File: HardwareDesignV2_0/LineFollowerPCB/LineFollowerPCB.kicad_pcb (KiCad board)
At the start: 2 copper layers, 152 x 100 mm, 11 parts, among them J1 B2B-XH-A, J2 B4B-XH-A, J3 Conn_01x04, M1 Motor_DC, M2 Motor_DC, U1 Black Pill v2, U2 DRV8833, U3 AMS1117-3.3, U4 SX1308

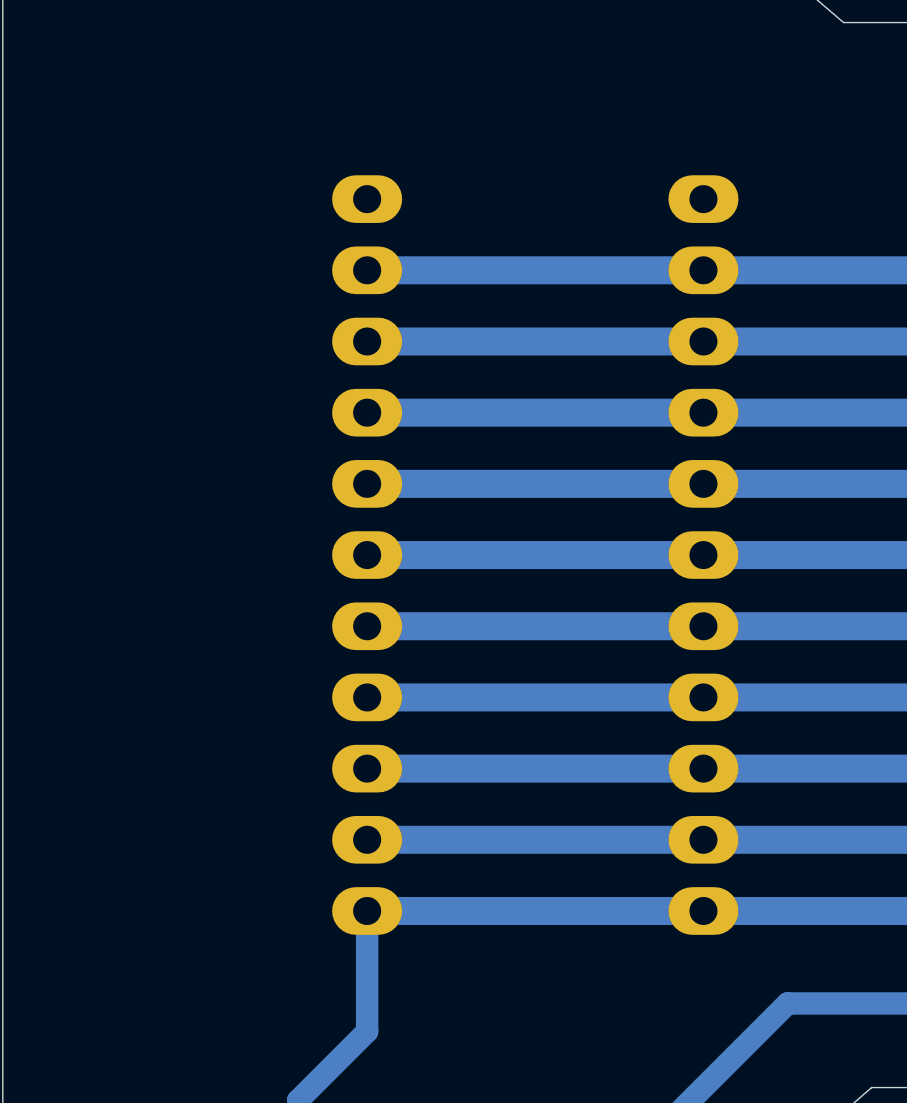
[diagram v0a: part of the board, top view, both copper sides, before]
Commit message: The LineFollower PCB design Version 2.0 with Cytron sensor
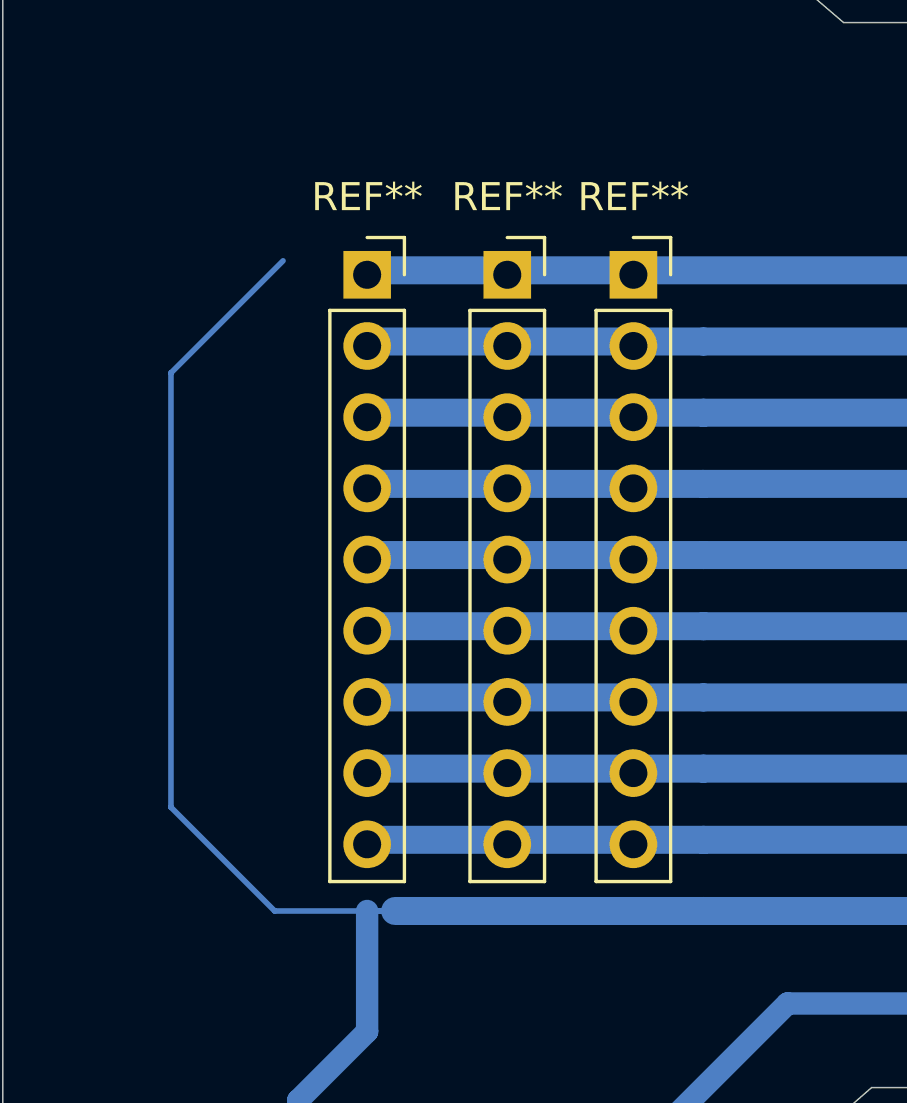
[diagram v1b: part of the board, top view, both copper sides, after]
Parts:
- removed U5, U6: ~, Connector_PinHeader_2.54mm:PinHeader_1x11_P2.54mm_Vertical
- added REF**: PinSocket_1x09_P2.54mm_Vertical, Connector_PinSocket_2.54mm:PinSocket_1x09_P2.54mm_Vertical, F.Cu at (88.0, 79.0)
- added REF**: PinSocket_1x09_P2.54mm_Vertical, Connector_PinSocket_2.54mm:PinSocket_1x09_P2.54mm_Vertical, F.Cu at (92.5, 79.0)
- added REF**: PinSocket_1x09_P2.54mm_Vertical, Connector_PinSocket_2.54mm:PinSocket_1x09_P2.54mm_Vertical, F.Cu at (83.0, 79.0)
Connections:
- U1 pad 26: IR_SG -> VCC
- U1 pad 27: D1 -> GND
- U1 pad 28: D2 -> AN
- U1 pad 29: D3 -> CAL
- U1 pad 30: D4 -> D1
- U1 pad 31: D5 -> D2
- U1 pad 32: D6 -> D3
- U1 pad 33: D7 -> D4
- U1 pad 34: D8 -> D5
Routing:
- net VCC: track 0.00 -> 90.5 mm
- net IR_SG: track 90.5 -> 0.00 mm
- net GND: track 0.00 -> 90.5 mm
- net D8: track 90.5 -> 0.00 mm
- net D7: track 90.5 -> 0.00 mm
- net D6: track 90.5 -> 0.00 mm
- net CAL: track 0.00 -> 90.5 mm
- net AN: track 0.00 -> 90.5 mm
- net IR_3.3V: track 122.3 -> 153.0 mm

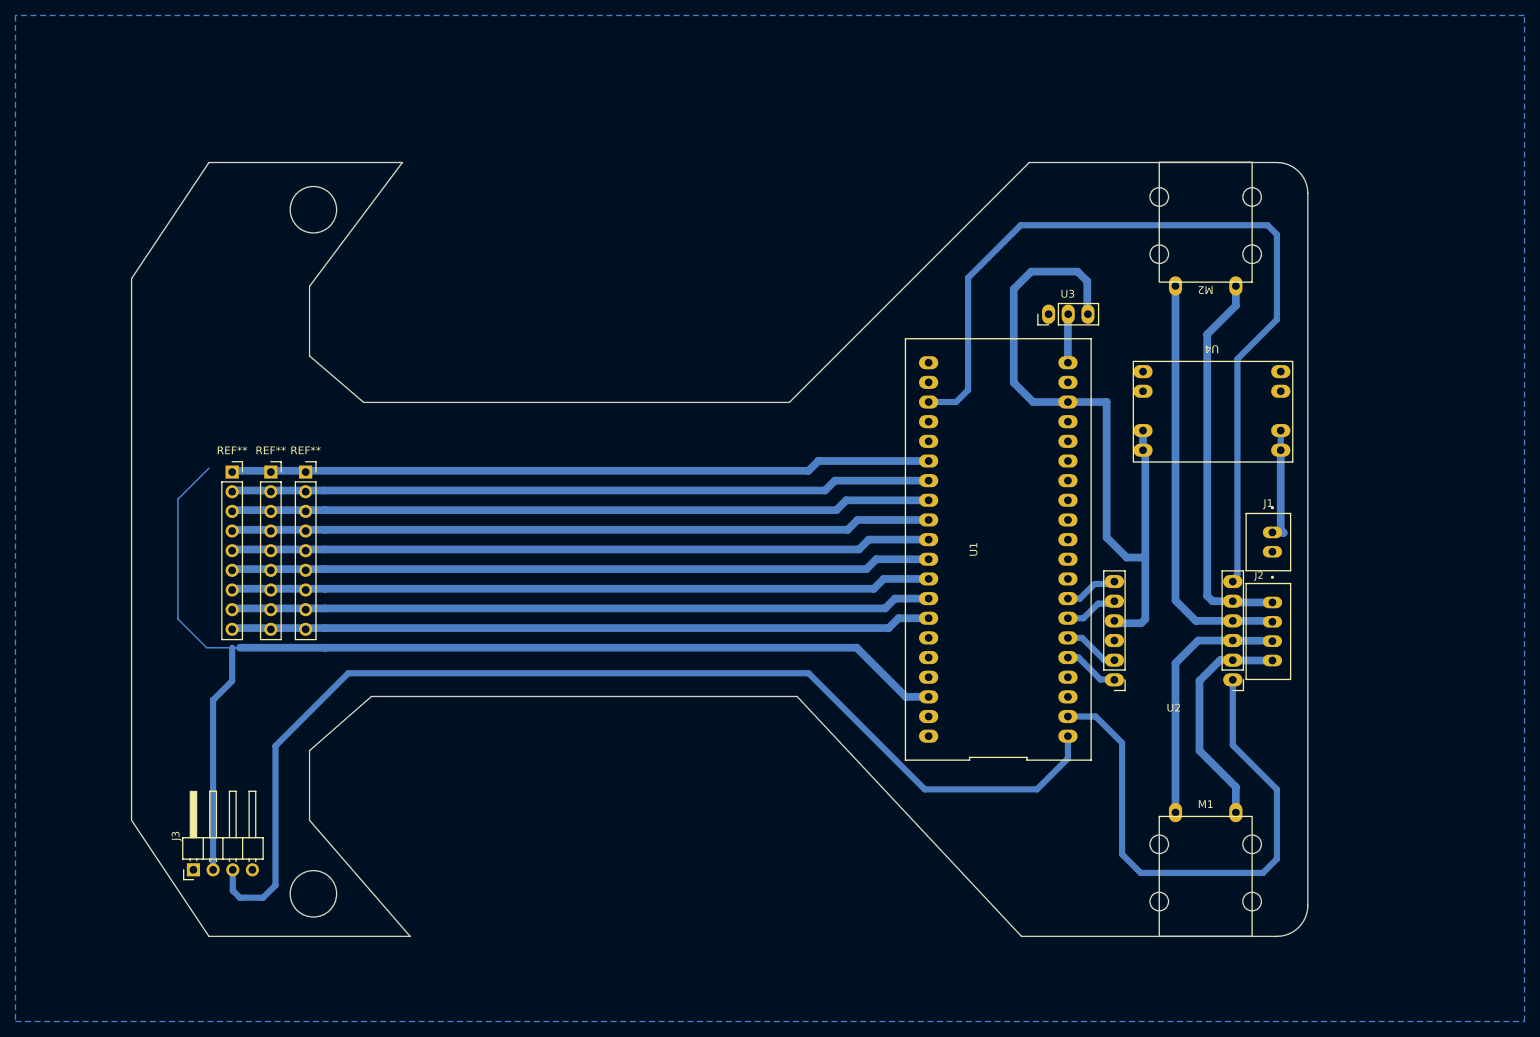
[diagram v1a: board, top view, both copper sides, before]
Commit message: - Update the schematic design - Fix the pins arrangment of the cytron sensor - Create the Cytron sensor footprint - Add the Cytron sensor 3D model - Add the 1N4001 doide - Update the layout
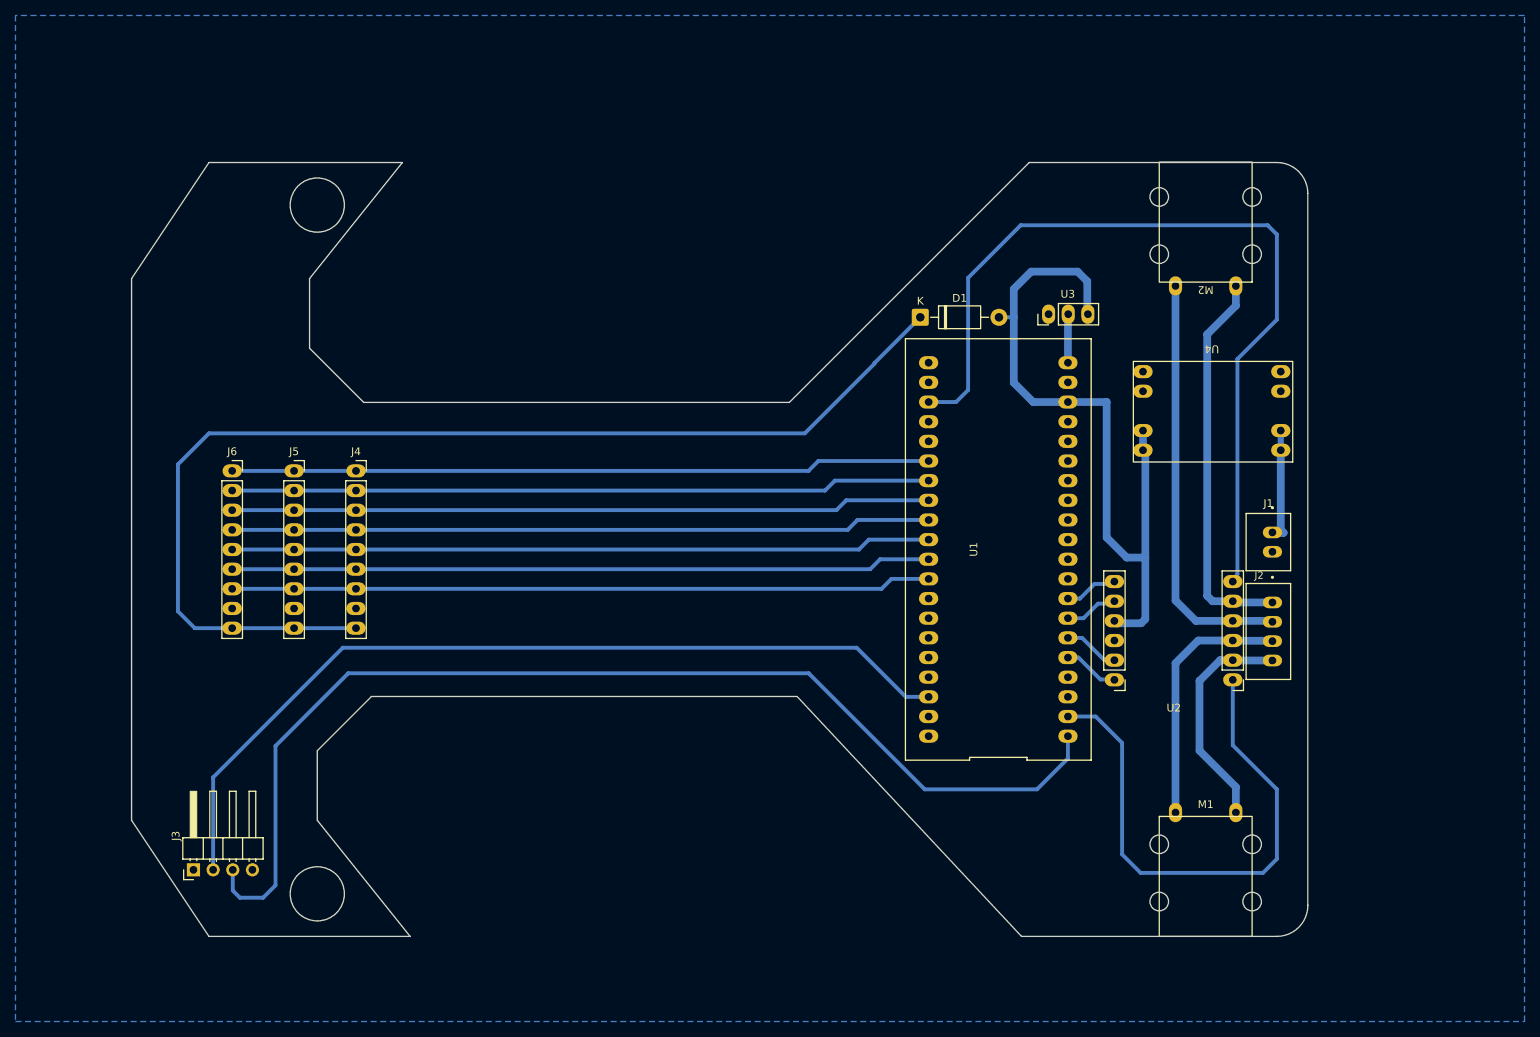
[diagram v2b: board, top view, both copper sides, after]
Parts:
- removed REF** (x3): PinSocket_1x09_P2.54mm_Vertical, Connector_PinSocket_2.54mm:PinSocket_1x09_P2.54mm_Vertical
- added D1: 1N4001, Diode_THT:D_DO-41_SOD81_P10.16mm_Horizontal, F.Cu at (171.9, 59.0)
- added J4: Conn_01x09, CytronLineMaker:CytronIR_Sensor, F.Cu at (99.0, 78.8)
- added J5: Conn_01x09, CytronLineMaker:CytronIR_Sensor, F.Cu at (91.0, 78.8)
- added J6: Conn_01x09, CytronLineMaker:CytronIR_Sensor, F.Cu at (83.0, 78.8)
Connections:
- net IR_3.3V renamed Neo_3.3V
- U1 pad 26: VCC -> D5
- U1 pad 27: GND -> D4
- U1 pad 28: AN -> D3
- U1 pad 29: CAL -> D2
- U1 pad 31: D2 -> CAL
- U1 pad 32: D3 -> AN
- U1 pad 33: D4 -> unconnected-(U1-PA7-Pad33)
- U1 pad 34: D5 -> unconnected-(U1-PB0-Pad34)
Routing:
- net GND: track 90.5 -> 0.00 mm
- net VCC: track 90.5 -> 146.7 mm
- net Neo_3.3V: track 153.0 -> 114.0 mm
- net 5.5V: track 92.8 -> 94.7 mm
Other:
- outline, holes or cut-outs redrawn
